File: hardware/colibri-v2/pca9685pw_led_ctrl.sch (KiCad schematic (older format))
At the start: 17 parts

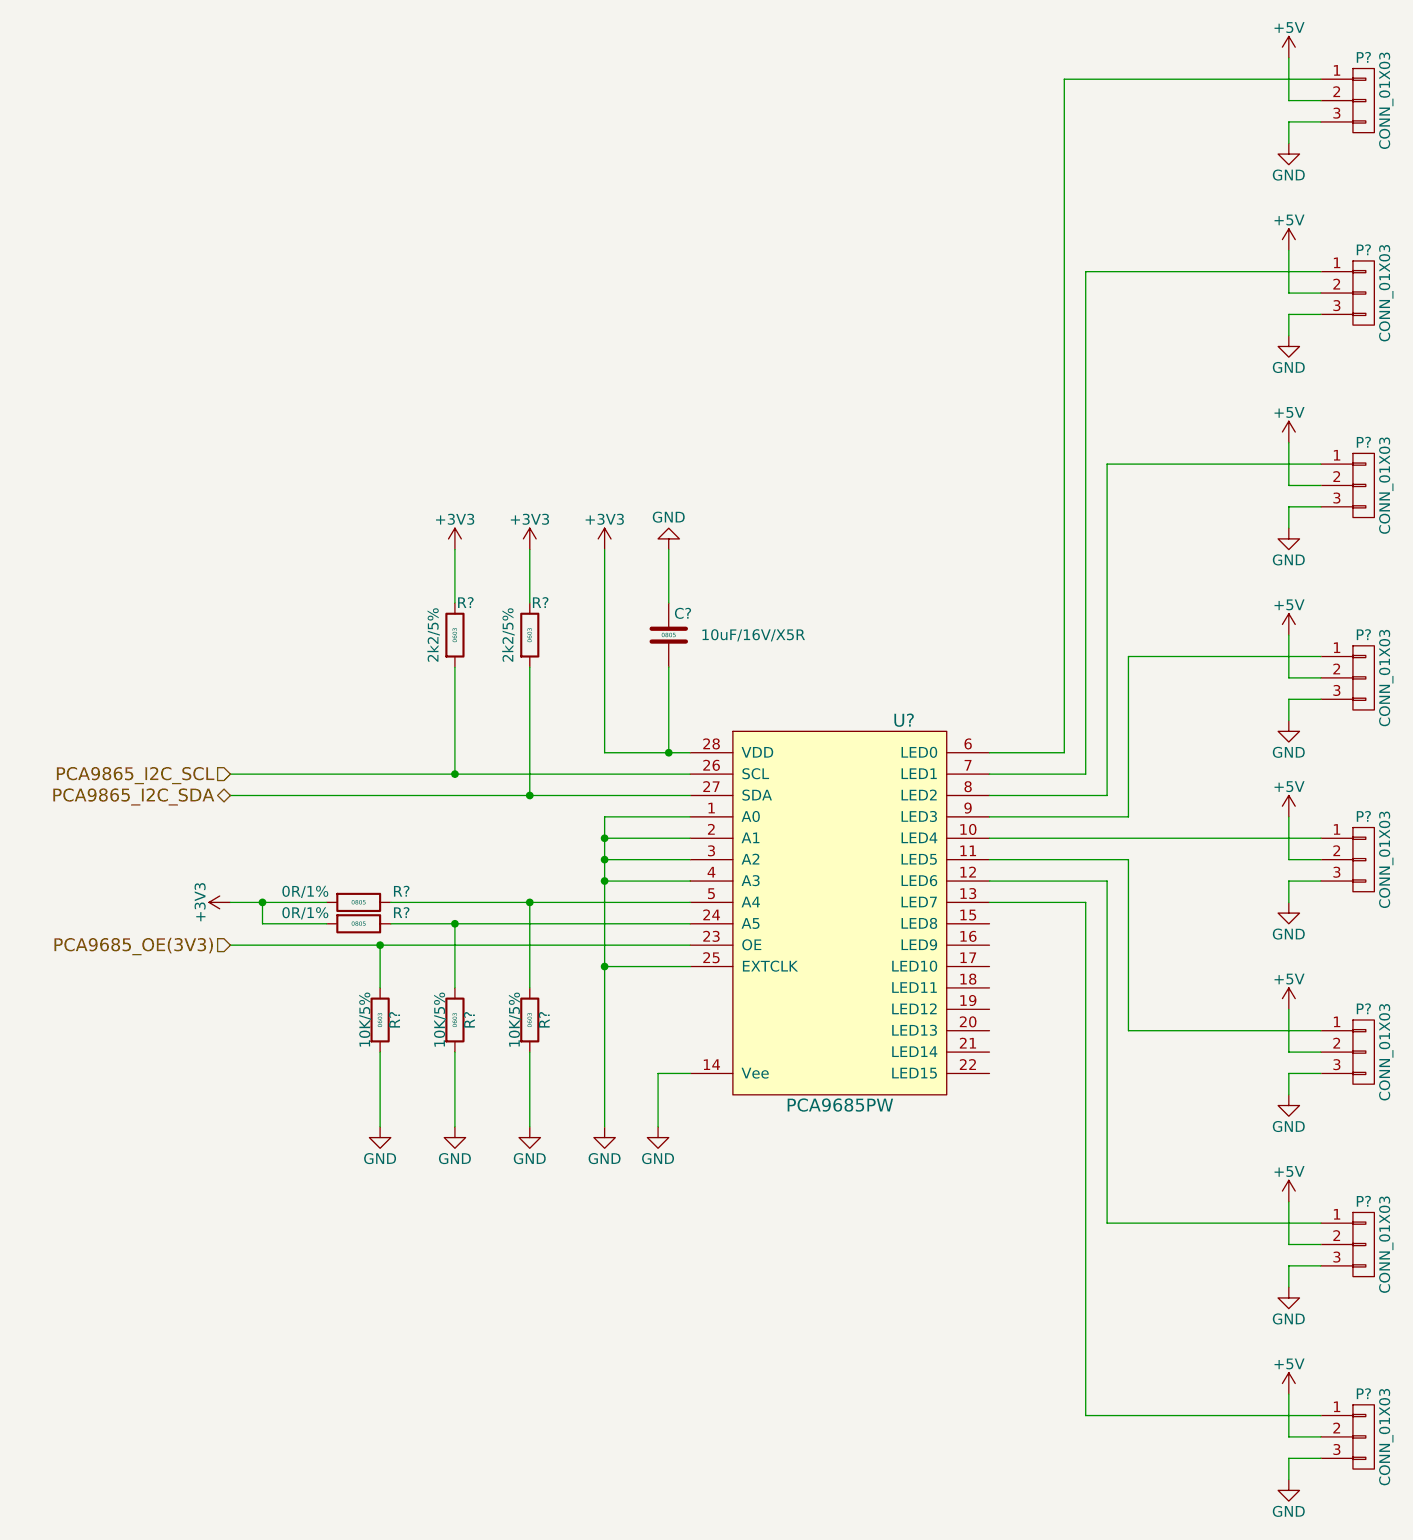
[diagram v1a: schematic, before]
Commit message: Resolving ERC problems
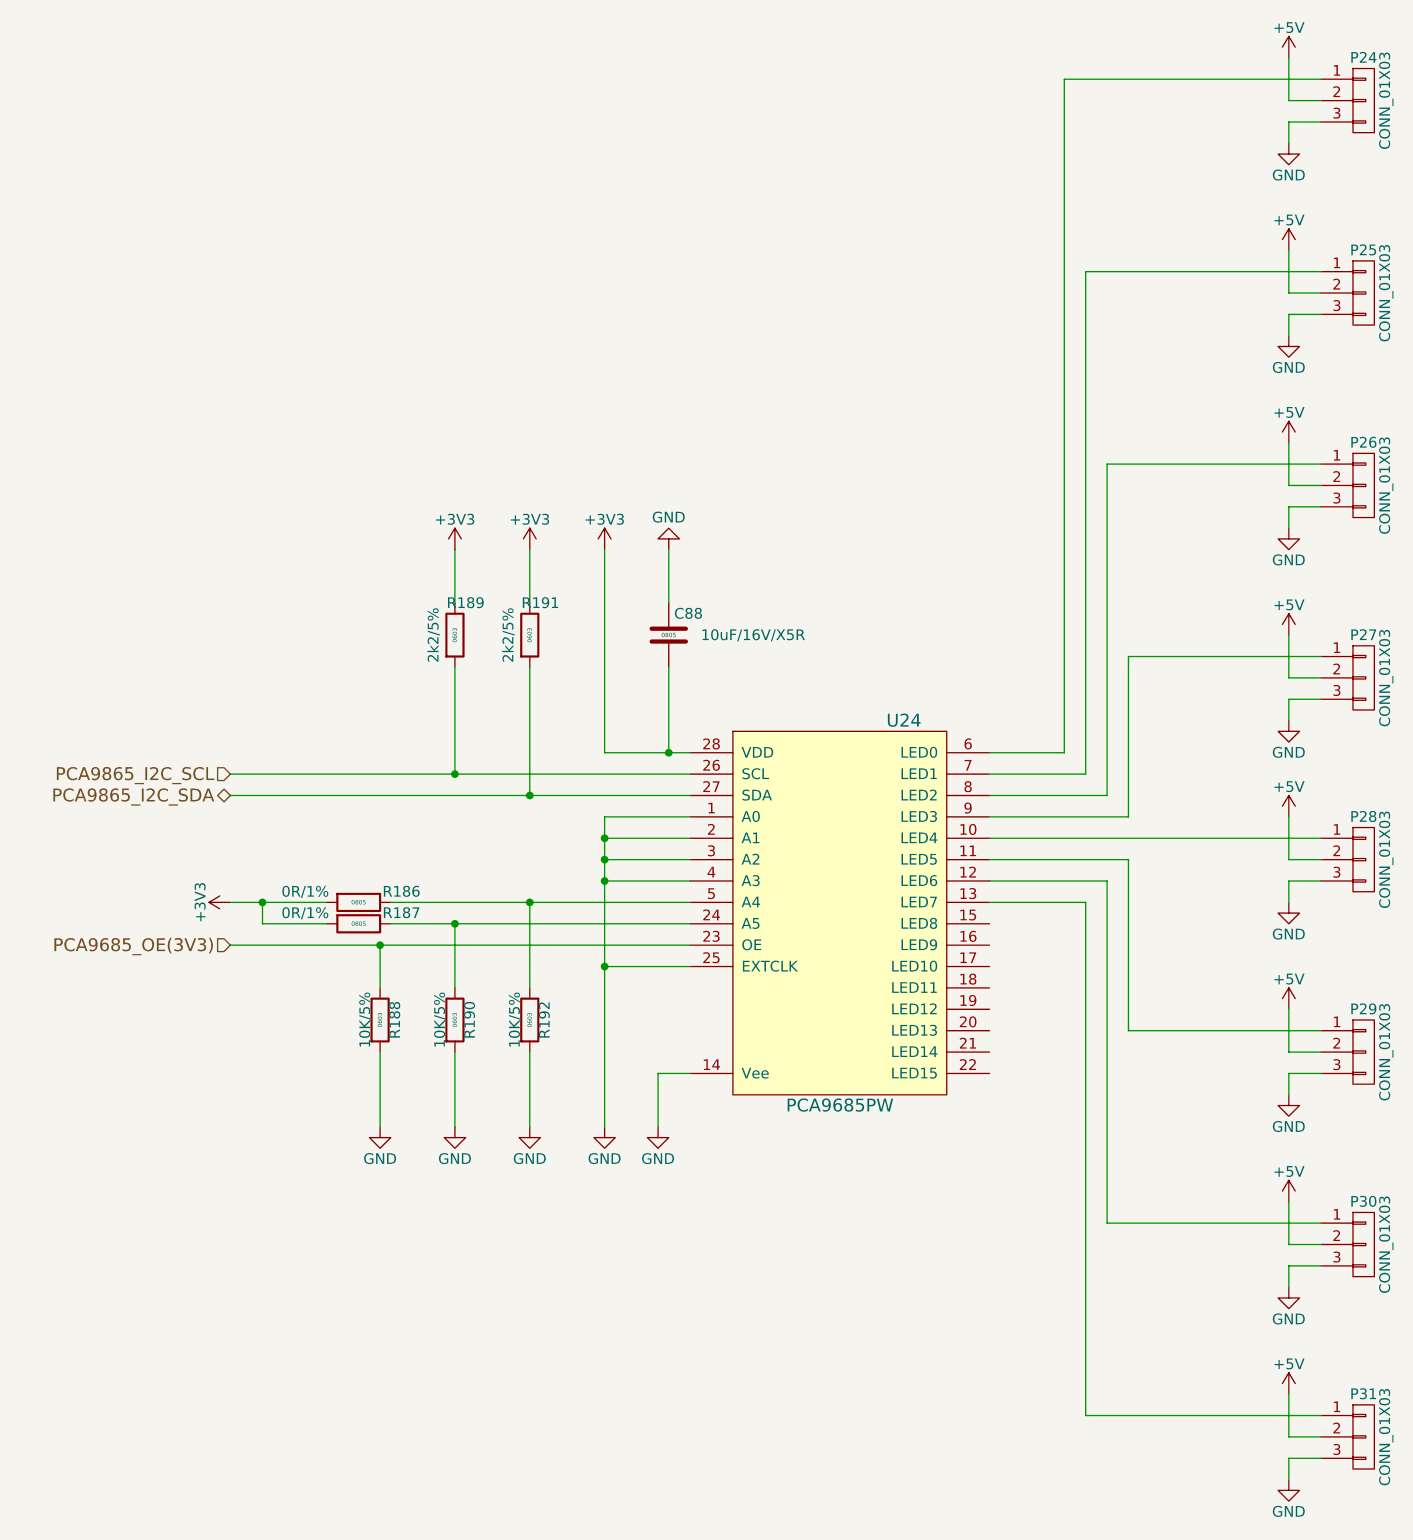
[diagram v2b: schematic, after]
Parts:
- gave numbers to parts that had none: 17

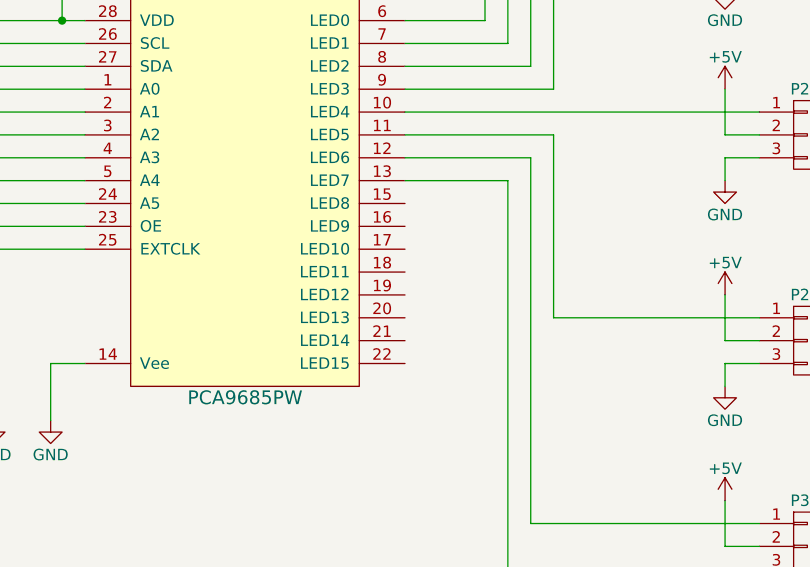
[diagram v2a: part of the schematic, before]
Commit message: Fixed ERC errors
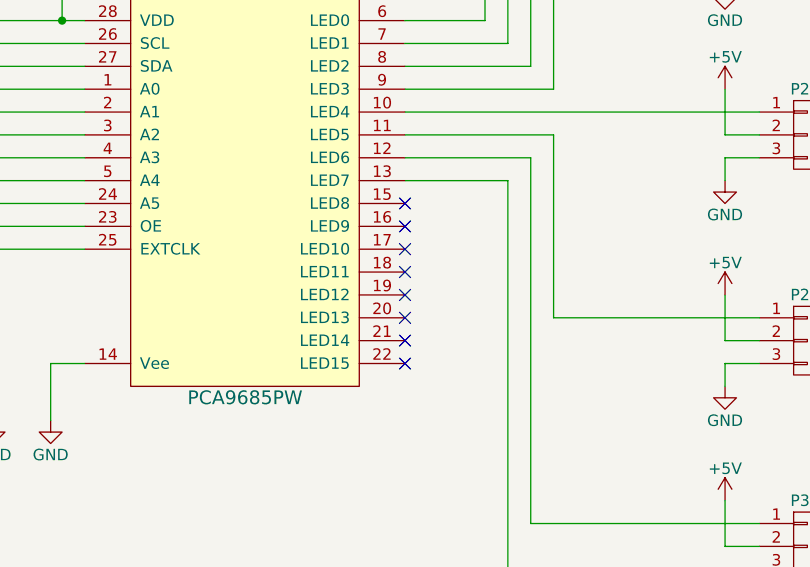
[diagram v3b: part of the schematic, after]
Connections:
- no-connect marks 0 -> 8
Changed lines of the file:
@@
 $EndComp
 $Comp
-L +5V #PWR0283
+L +5V #PWR0273
 U 1 1 566CC35F
 P 6350 4350
-F 0 "#PWR0283" H 6350 4200 50  0001 C CNN
+F 0 "#PWR0273" H 6350 4200 50  0001 C CNN
 F 1 "+5V" H 6350 4490 50  0000 C CNN
 F 2 "" H 6350 4350 60  0000 C CNN
@@
 $EndComp
 $Comp
-L GND #PWR0284
+L GND #PWR0274
 U 1 1 566CC365
 P 6350 4750
-F 0 "#PWR0284" H 6350 4500 50  0001 C CNN
+F 0 "#PWR0274" H 6350 4500 50  0001 C CNN
 F 1 "GND" H 6350 4600 50  0000 C CNN
 F 2 "" H 6350 4750 60  0000 C CNN
@@
 $EndComp
 $Comp
-L +5V #PWR0285
+L +5V #PWR0275
 U 1 1 566CC372
 P 6350 5250
-F 0 "#PWR0285" H 6350 5100 50  0001 C CNN
+F 0 "#PWR0275" H 6350 5100 50  0001 C CNN
 F 1 "+5V" H 6350 5390 50  0000 C CNN
 F 2 "" H 6350 5250 60  0000 C CNN
@@
 $EndComp
 $Comp
-L GND #PWR0286
+L GND #PWR0276
 U 1 1 566CC378
 P 6350 5650
-F 0 "#PWR0286" H 6350 5400 50  0001 C CNN
+F 0 "#PWR0276" H 6350 5400 50  0001 C CNN
 F 1 "GND" H 6350 5500 50  0000 C CNN
 F 2 "" H 6350 5650 60  0000 C CNN
@@
 $EndComp
 $Comp
-L +5V #PWR0287
+L +5V #PWR0277
 U 1 1 566CC385
 P 6350 6150
-F 0 "#PWR0287" H 6350 6000 50  0001 C CNN
+F 0 "#PWR0277" H 6350 6000 50  0001 C CNN
 F 1 "+5V" H 6350 6290 50  0000 C CNN
 F 2 "" H 6350 6150 60  0000 C CNN
@@
 $EndComp
 $Comp
-L GND #PWR0288
+L GND #PWR0278
 U 1 1 566CC38B
 P 6350 6550
-F 0 "#PWR0288" H 6350 6300 50  0001 C CNN
+F 0 "#PWR0278" H 6350 6300 50  0001 C CNN
 F 1 "GND" H 6350 6400 50  0000 C CNN
 F 2 "" H 6350 6550 60  0000 C CNN
@@
 $EndComp
 $Comp
-L +5V #PWR0289
+L +5V #PWR0279
 U 1 1 566CC398
 P 6350 7050
-F 0 "#PWR0289" H 6350 6900 50  0001 C CNN
+F 0 "#PWR0279" H 6350 6900 50  0001 C CNN
 F 1 "+5V" H 6350 7190 50  0000 C CNN
 F 2 "" H 6350 7050 60  0000 C CNN
@@
 $EndComp
 $Comp
-L GND #PWR0290
+L GND #PWR0280
 U 1 1 566CC39E
 P 6350 7450
-F 0 "#PWR0290" H 6350 7200 50  0001 C CNN
+F 0 "#PWR0280" H 6350 7200 50  0001 C CNN
 F 1 "GND" H 6350 7300 50  0000 C CNN
 F 2 "" H 6350 7450 60  0000 C CNN
@@
 $EndComp
 $Comp
-L +5V #PWR0291
+L +5V #PWR0281
 U 1 1 566CC3AB
 P 6350 800
-F 0 "#PWR0291" H 6350 650 50  0001 C CNN
+F 0 "#PWR0281" H 6350 650 50  0001 C CNN
 F 1 "+5V" H 6350 940 50  0000 C CNN
 F 2 "" H 6350 800 60  0000 C CNN
@@
 $EndComp
 $Comp
-L GND #PWR0292
+L GND #PWR0282
 U 1 1 566CC3B1
 P 6350 1200
-F 0 "#PWR0292" H 6350 950 50  0001 C CNN
+F 0 "#PWR0282" H 6350 950 50  0001 C CNN
 F 1 "GND" H 6350 1050 50  0000 C CNN
 F 2 "" H 6350 1200 60  0000 C CNN
@@
 $EndComp
 $Comp
-L +5V #PWR0293
+L +5V #PWR0283
 U 1 1 566CC3BE
 P 6350 1700
-F 0 "#PWR0293" H 6350 1550 50  0001 C CNN
+F 0 "#PWR0283" H 6350 1550 50  0001 C CNN
 F 1 "+5V" H 6350 1840 50  0000 C CNN
 F 2 "" H 6350 1700 60  0000 C CNN
@@
 $EndComp
 $Comp
-L GND #PWR0294
+L GND #PWR0284
 U 1 1 566CC3C4
 P 6350 2100
-F 0 "#PWR0294" H 6350 1850 50  0001 C CNN
+F 0 "#PWR0284" H 6350 1850 50  0001 C CNN
 F 1 "GND" H 6350 1950 50  0000 C CNN
 F 2 "" H 6350 2100 60  0000 C CNN
@@
 $EndComp
 $Comp
-L +5V #PWR0295
+L +5V #PWR0285
 U 1 1 566CC3D1
 P 6350 2600
-F 0 "#PWR0295" H 6350 2450 50  0001 C CNN
+F 0 "#PWR0285" H 6350 2450 50  0001 C CNN
 F 1 "+5V" H 6350 2740 50  0000 C CNN
 F 2 "" H 6350 2600 60  0000 C CNN
@@
 $EndComp
 $Comp
-L GND #PWR0296
+L GND #PWR0286
 U 1 1 566CC3D7
 P 6350 3000
-F 0 "#PWR0296" H 6350 2750 50  0001 C CNN
+F 0 "#PWR0286" H 6350 2750 50  0001 C CNN
 F 1 "GND" H 6350 2850 50  0000 C CNN
 F 2 "" H 6350 3000 60  0000 C CNN
@@
 $EndComp
 $Comp
-L +5V #PWR0297
+L +5V #PWR0287
 U 1 1 566CC3E4
 P 6350 3500
-F 0 "#PWR0297" H 6350 3350 50  0001 C CNN
+F 0 "#PWR0287" H 6350 3350 50  0001 C CNN
 F 1 "+5V" H 6350 3640 50  0000 C CNN
 F 2 "" H 6350 3500 60  0000 C CNN
@@
 $EndComp
 $Comp
-L GND #PWR0298
+L GND #PWR0288
 U 1 1 566CC3EA
 P 6350 3900
-F 0 "#PWR0298" H 6350 3650 50  0001 C CNN
+F 0 "#PWR0288" H 6350 3650 50  0001 C CNN
 F 1 "GND" H 6350 3750 50  0000 C CNN
 F 2 "" H 6350 3900 60  0000 C CNN
@@
 	1400 4950 3550 4950
 $Comp
-L GND #PWR0299
+L GND #PWR0289
 U 1 1 566D160D
 P 3400 5800
-F 0 "#PWR0299" H 3400 5550 50  0001 C CNN
+F 0 "#PWR0289" H 3400 5550 50  0001 C CNN
 F 1 "GND" H 3400 5650 50  0000 C CNN
 F 2 "" H 3400 5800 50  0000 C CNN
@@
 	3400 5550 3400 5800
 $Comp
-L GND #PWR0300
+L GND #PWR0290
 U 1 1 566D16B1
 P 3150 5800
-F 0 "#PWR0300" H 3150 5550 50  0001 C CNN
+F 0 "#PWR0290" H 3150 5550 50  0001 C CNN
 F 1 "GND" H 3150 5650 50  0000 C CNN
 F 2 "" H 3150 5800 50  0000 C CNN
@@
 Connection ~ 3150 4450
 $Comp
-L +3V3 #PWR0301
+L +3V3 #PWR0291
 U 1 1 566D18F8
 P 3150 3100
-F 0 "#PWR0301" H 3150 2950 50  0001 C CNN
+F 0 "#PWR0291" H 3150 2950 50  0001 C CNN
 F 1 "+3V3" H 3150 3240 50  0000 C CNN
 F 2 "" H 3150 3100 50  0000 C CNN
@@
 	3450 3100 3450 3350
 $Comp
-L GND #PWR0302
+L GND #PWR0292
 U 1 1 566D19F4
 P 3450 3100
-F 0 "#PWR0302" H 3450 2850 50  0001 C CNN
+F 0 "#PWR0292" H 3450 2850 50  0001 C CNN
 F 1 "GND" H 3450 2950 50  0000 C CNN
 F 2 "" H 3450 3100 50  0000 C CNN
@@
 $EndComp
 $Comp
-L +3V3 #PWR0303
+L +3V3 #PWR0293
 U 1 1 566D1D19
 P 2800 3100
-F 0 "#PWR0303" H 2800 2950 50  0001 C CNN
+F 0 "#PWR0293" H 2800 2950 50  0001 C CNN
 F 1 "+3V3" H 2800 3240 50  0000 C CNN
 F 2 "" H 2800 3100 50  0000 C CNN
@@
 $EndComp
 $Comp
-L +3V3 #PWR0304
+L +3V3 #PWR0294
 U 1 1 566D1D57
 P 2450 3100
-F 0 "#PWR0304" H 2450 2950 50  0001 C CNN
+F 0 "#PWR0294" H 2450 2950 50  0001 C CNN
 F 1 "+3V3" H 2450 3240 50  0000 C CNN
 F 2 "" H 2450 3100 50  0000 C CNN
@@
 Connection ~ 3450 4050
 $Comp
-L +3V3 #PWR0305
+L +3V3 #PWR0295
 U 1 1 566D2184
 P 1400 4750
-F 0 "#PWR0305" H 1400 4600 50  0001 C CNN
+F 0 "#PWR0295" H 1400 4600 50  0001 C CNN
 F 1 "+3V3" H 1400 4890 50  0000 C CNN
 F 2 "" H 1400 4750 50  0000 C CNN
@@
 Connection ~ 2100 4950
 $Comp
-L GND #PWR0306
+L GND #PWR0296
 U 1 1 566D271C
 P 2800 5800
-F 0 "#PWR0306" H 2800 5550 50  0001 C CNN
+F 0 "#PWR0296" H 2800 5550 50  0001 C CNN
 F 1 "GND" H 2800 5650 50  0000 C CNN
 F 2 "" H 2800 5800 50  0000 C CNN
@@
 $EndComp
 $Comp
-L GND #PWR0307
+L GND #PWR0297
 U 1 1 566D275A
 P 2450 5800
-F 0 "#PWR0307" H 2450 5550 50  0001 C CNN
+F 0 "#PWR0297" H 2450 5550 50  0001 C CNN
 F 1 "GND" H 2450 5650 50  0000 C CNN
 F 2 "" H 2450 5800 50  0000 C CNN
@@
 $EndComp
 $Comp
-L GND #PWR0308
+L GND #PWR0298
 U 1 1 566D2798
 P 2100 5800
-F 0 "#PWR0308" H 2100 5550 50  0001 C CNN
+F 0 "#PWR0298" H 2100 5550 50  0001 C CNN
 F 1 "GND" H 2100 5650 50  0000 C CNN
 F 2 "" H 2100 5800 50  0000 C CNN
@@
 Wire Wire Line
 	2100 5450 2100 5800
+NoConn ~ 4950 4850
+NoConn ~ 4950 4950
+NoConn ~ 4950 5050
+NoConn ~ 4950 5150
+NoConn ~ 4950 5250
+NoConn ~ 4950 5350
+NoConn ~ 4950 5450
+NoConn ~ 4950 5550
 $EndSCHEMATC
